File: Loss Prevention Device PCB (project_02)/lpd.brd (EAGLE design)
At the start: 48.3 x 58.4 mm, 4 parts, among them U2 GT-U7, U3 HM-10

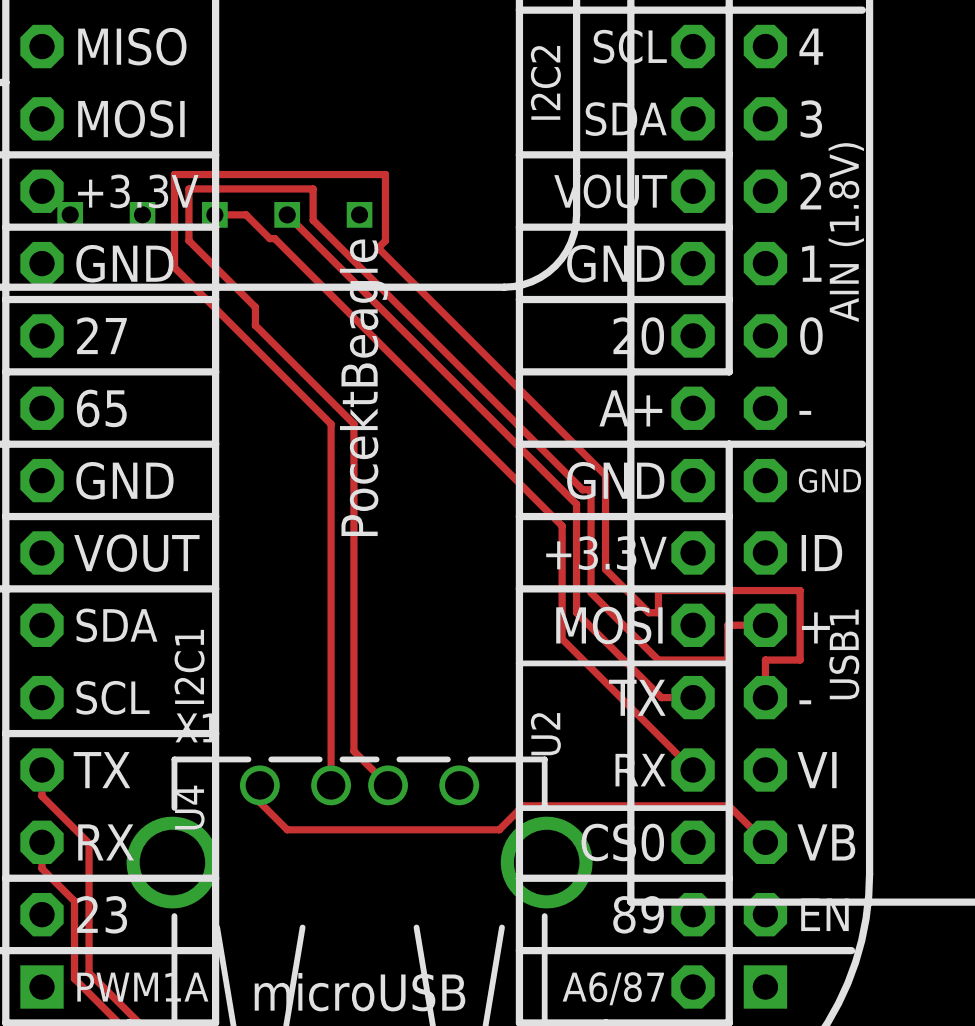
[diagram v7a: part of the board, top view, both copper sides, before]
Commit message: Matched USB connection lengths
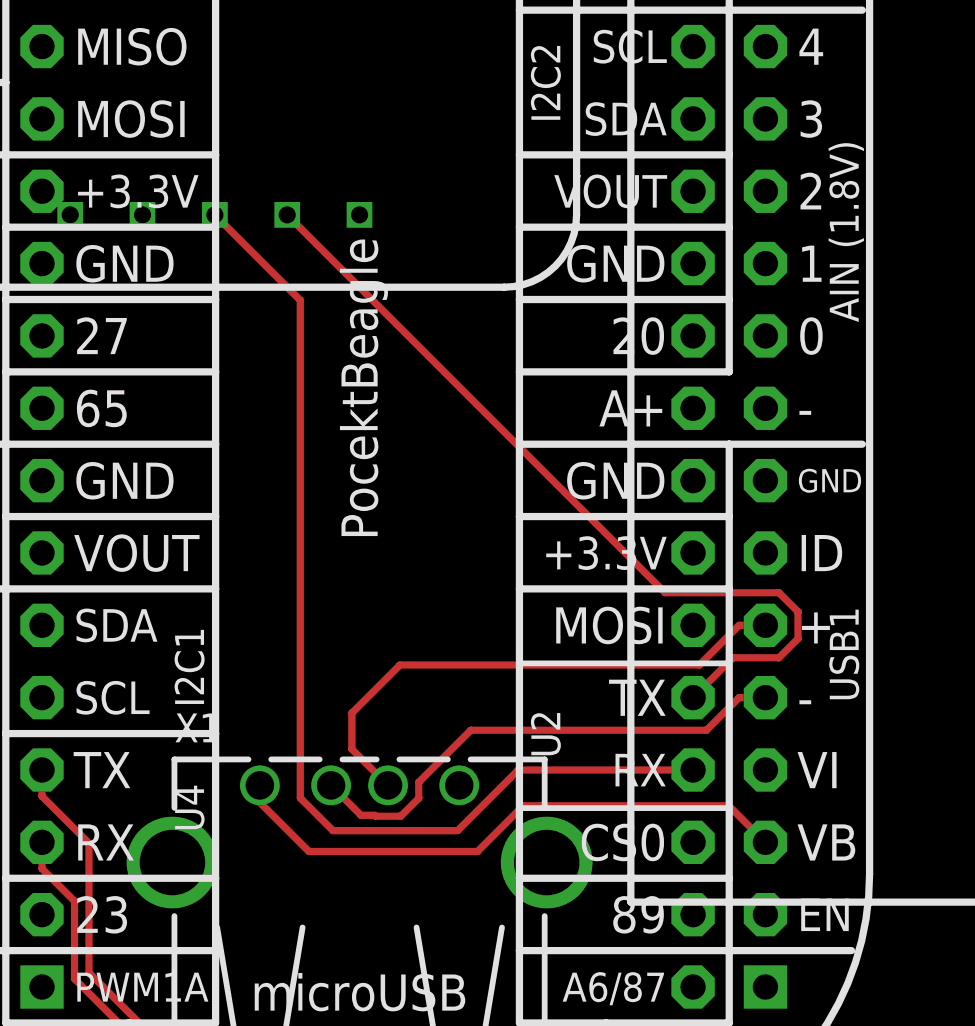
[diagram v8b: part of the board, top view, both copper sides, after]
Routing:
- net USB1.D-: track 61.6 -> 17.7 mm
- net USB1.D+: track 54.9 -> 18.9 mm
- net UART2.RX: track 27.2 -> 36.9 mm
- net UART2.TX: track 23.5 -> 29.2 mm
- net USB1.VBUS: track 19.6 -> 20.3 mm
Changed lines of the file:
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@@
 <setting verticaltext="up"/>
 </settings>
-<grid distance="100" unitdist="mil" unit="mil" style="lines" multiple="1" display="yes" altdistance="5" altunitdist="mil" altunit="mil"/>
+<grid distance="10" unitdist="mil" unit="mil" style="lines" multiple="1" display="yes" altdistance="5" altunitdist="mil" altunit="mil"/>
 <layers>
 <layer number="1" name="Top" color="4" fill="1" visible="yes" active="yes"/>
@@
 <contactref element="U2" pad="P$3"/>
 <contactref element="U$1" pad="P1_08"/>
-<wire x1="32.03" y1="14.8" x2="27.432" y2="19.398" width="0.254" layer="1"/>
-<wire x1="17.3434" y1="33.4566" x2="17.1697875" y2="33.4566" width="0.254" layer="1"/>
-<wire x1="16.3363875" y1="34.29" x2="15.24" y2="34.29" width="0.254" layer="1"/>
-<wire x1="17.1697875" y1="33.4566" x2="16.3363875" y2="34.29" width="0.254" layer="1"/>
-<wire x1="27.432" y1="19.398" x2="27.432" y2="23.368" width="0.254" layer="1"/>
-<wire x1="27.432" y1="23.368" x2="17.3434" y2="33.4566" width="0.254" layer="1"/>
+<wire x1="15.24" y1="34.29" x2="18.239" y2="31.291" width="0.254" layer="1"/>
+<wire x1="25.88876875" y1="14.8" x2="32.03" y2="14.8" width="0.254" layer="1"/>
+<wire x1="18.239" y1="31.291" x2="18.239" y2="13.81223125" width="0.254" layer="1"/>
+<wire x1="23.75976875" y1="12.671" x2="25.88876875" y2="14.8" width="0.254" layer="1"/>
+<wire x1="18.239" y1="13.81223125" x2="19.38023125" y2="12.671" width="0.254" layer="1"/>
+<wire x1="19.38023125" y1="12.671" x2="23.75976875" y2="12.671" width="0.254" layer="1"/>
 </signal>
 <signal name="UART2.TX">
 <contactref element="U2" pad="P$4"/>
 <contactref element="U$1" pad="P1_10"/>
-<wire x1="17.78" y1="34.29" x2="27.94" y2="24.13" width="0.254" layer="1"/>
-<wire x1="27.94" y1="24.13" x2="27.94" y2="20.32" width="0.254" layer="1"/>
-<wire x1="27.94" y1="20.32" x2="30.92" y2="17.34" width="0.254" layer="1"/>
-<wire x1="30.92" y1="17.34" x2="32.03" y2="17.34" width="0.254" layer="1"/>
+<wire x1="35.04345" y1="21.023" x2="35.713" y2="20.35345" width="0.254" layer="1"/>
+<wire x1="35.713" y1="20.35345" x2="35.713" y2="19.40655" width="0.254" layer="1"/>
+<wire x1="35.713" y1="19.40655" x2="35.04345" y2="18.737" width="0.254" layer="1"/>
+<wire x1="17.78" y1="34.29" x2="31.047" y2="21.023" width="0.254" layer="1"/>
+<wire x1="35.04345" y1="18.737" x2="33.427" y2="18.737" width="0.254" layer="1"/>
+<wire x1="33.427" y1="18.737" x2="32.03" y2="17.34" width="0.254" layer="1"/>
+<wire x1="31.047" y1="21.023" x2="35.04345" y2="21.023" width="0.254" layer="1"/>
 </signal>
 <signal name="UART4.TX">
@@
 <contactref element="X1" pad="1"/>
 <contactref element="U$1" pad="P1_05"/>
-<wire x1="26.0653" y1="13.5409" x2="25.2244" y2="12.7" width="0.254" layer="1"/>
-<wire x1="25.2244" y1="12.7" x2="17.78" y2="12.7" width="0.254" layer="1"/>
+<wire x1="26.0653" y1="13.5409" x2="24.4624" y2="11.938" width="0.254" layer="1"/>
+<wire x1="24.4624" y1="11.938" x2="18.542" y2="11.938" width="0.254" layer="1"/>
 <wire x1="34.57" y1="12.26" x2="33.2891" y2="13.5409" width="0.254" layer="1"/>
 <wire x1="33.2891" y1="13.5409" x2="26.0653" y2="13.5409" width="0.254" layer="1"/>
-<wire x1="17.78" y1="12.7" x2="16.82" y2="13.66" width="0.254" layer="1"/>
+<wire x1="18.542" y1="11.938" x2="16.82" y2="13.66" width="0.254" layer="1"/>
 <wire x1="16.82" y1="13.66" x2="16.82" y2="14.26" width="0.254" layer="1"/>
 </signal>
@@
 <contactref element="X1" pad="2"/>
 <contactref element="U$1" pad="P1_09"/>
-<wire x1="34.57" y1="17.34" x2="34.57" y2="18.6608" width="0.254" layer="1"/>
-<wire x1="34.57" y1="18.6608" x2="35.7892" y2="18.6608" width="0.254" layer="1"/>
-<wire x1="35.7892" y1="18.6608" x2="35.7892" y2="21.0992" width="0.254" layer="1"/>
-<wire x1="30.8108" y1="21.0992" x2="30.8108" y2="20.32" width="0.254" layer="1"/>
-<wire x1="30.8108" y1="20.32" x2="30.48" y2="20.32" width="0.254" layer="1"/>
-<wire x1="35.7892" y1="21.0992" x2="30.8108" y2="21.0992" width="0.254" layer="1"/>
-<wire x1="30.48" y1="20.32" x2="28.956" y2="21.844" width="0.254" layer="1"/>
-<wire x1="28.956" y1="21.844" x2="28.956" y2="25.146" width="0.254" layer="1"/>
-<wire x1="28.956" y1="25.146" x2="20.9756" y2="33.1264" width="0.254" layer="1"/>
-<wire x1="20.9756" y1="33.1264" x2="21.2296" y2="33.3804" width="0.254" layer="1"/>
-<wire x1="21.2296" y1="33.3804" x2="21.2296" y2="35.7076" width="0.254" layer="1"/>
-<wire x1="21.2296" y1="35.7076" x2="13.8224" y2="35.7076" width="0.254" layer="1"/>
-<wire x1="13.8224" y1="35.7076" x2="13.8224" y2="32.4406" width="0.254" layer="1"/>
-<wire x1="13.8224" y1="32.4406" x2="19.32" y2="26.943" width="0.254" layer="1"/>
-<wire x1="19.32" y1="26.943" x2="19.32" y2="14.26" width="0.254" layer="1"/>
+<wire x1="34.57" y1="17.34" x2="33.64645" y2="17.34" width="0.254" layer="1"/>
+<wire x1="33.64645" y1="17.34" x2="32.50345" y2="16.197" width="0.254" layer="1"/>
+<wire x1="32.50345" y1="16.197" x2="24.22823125" y2="16.197" width="0.254" layer="1"/>
+<wire x1="24.22823125" y1="16.197" x2="22.401" y2="14.36976875" width="0.254" layer="1"/>
+<wire x1="22.401" y1="13.81223125" x2="22.401" y2="14.36976875" width="0.254" layer="1"/>
+<wire x1="19.32" y1="14.26" x2="20.372" y2="13.208" width="0.254" layer="1"/>
+<wire x1="20.84323125" y1="13.208" x2="20.87223125" y2="13.179" width="0.254" layer="1"/>
+<wire x1="20.87223125" y1="13.179" x2="21.76776875" y2="13.179" width="0.254" layer="1"/>
+<wire x1="20.372" y1="13.208" x2="20.84323125" y2="13.208" width="0.254" layer="1"/>
+<wire x1="21.76776875" y1="13.179" x2="22.401" y2="13.81223125" width="0.254" layer="1"/>
 </signal>
 <signal name="USB1.D+">
 <contactref element="X1" pad="3"/>
 <contactref element="U$1" pad="P1_11"/>
-<wire x1="34.57" y1="19.88" x2="33.2492" y2="19.88" width="0.254" layer="1"/>
-<wire x1="33.2492" y1="19.88" x2="33.2492" y2="18.6608" width="0.254" layer="1"/>
-<wire x1="33.2492" y1="18.6608" x2="30.8108" y2="18.6608" width="0.254" layer="1"/>
-<wire x1="14.3304" y1="35.1996" x2="14.3304" y2="33.3804" width="0.254" layer="1"/>
-<wire x1="16.6617875" y1="31.0490125" x2="16.6617875" y2="30.4086" width="0.254" layer="1"/>
-<wire x1="14.3304" y1="33.3804" x2="16.6617875" y2="31.0490125" width="0.254" layer="1"/>
-<wire x1="28.448" y1="24.638" x2="28.1528" y2="24.638" width="0.254" layer="1"/>
-<wire x1="28.1528" y1="24.638" x2="18.6896" y2="34.1012" width="0.254" layer="1"/>
-<wire x1="18.6896" y1="34.1012" x2="18.6896" y2="35.1996" width="0.254" layer="1"/>
-<wire x1="16.6617875" y1="30.4086" x2="20.1228" y2="26.9475875" width="0.254" layer="1"/>
-<wire x1="20.1228" y1="26.9475875" x2="20.1228" y2="15.4572" width="0.254" layer="1"/>
-<wire x1="21.32" y1="14.26" x2="20.1228" y2="15.4572" width="0.254" layer="1"/>
-<wire x1="30.8108" y1="18.6608" x2="28.448" y2="21.0236" width="0.254" layer="1"/>
-<wire x1="28.448" y1="21.0236" x2="28.448" y2="24.638" width="0.254" layer="1"/>
-<wire x1="18.6896" y1="35.1996" x2="14.3304" y2="35.1996" width="0.254" layer="1"/>
+<wire x1="34.57" y1="19.88" x2="33.64645" y2="19.88" width="0.254" layer="1"/>
+<wire x1="33.64645" y1="19.88" x2="32.24945" y2="18.483" width="0.254" layer="1"/>
+<wire x1="21.733" y1="18.483" x2="20.05" y2="16.8" width="0.254" layer="1"/>
+<wire x1="20.05" y1="16.8" x2="20.05" y2="15.53" width="0.254" layer="1"/>
+<wire x1="20.05" y1="15.53" x2="21.32" y2="14.26" width="0.254" layer="1"/>
+<wire x1="32.24945" y1="18.483" x2="21.733" y2="18.483" width="0.254" layer="1"/>
 </signal>
 <signal name="VIN">
